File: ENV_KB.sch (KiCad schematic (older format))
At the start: 183 parts, among them J1 TYPE-C-31-M-12

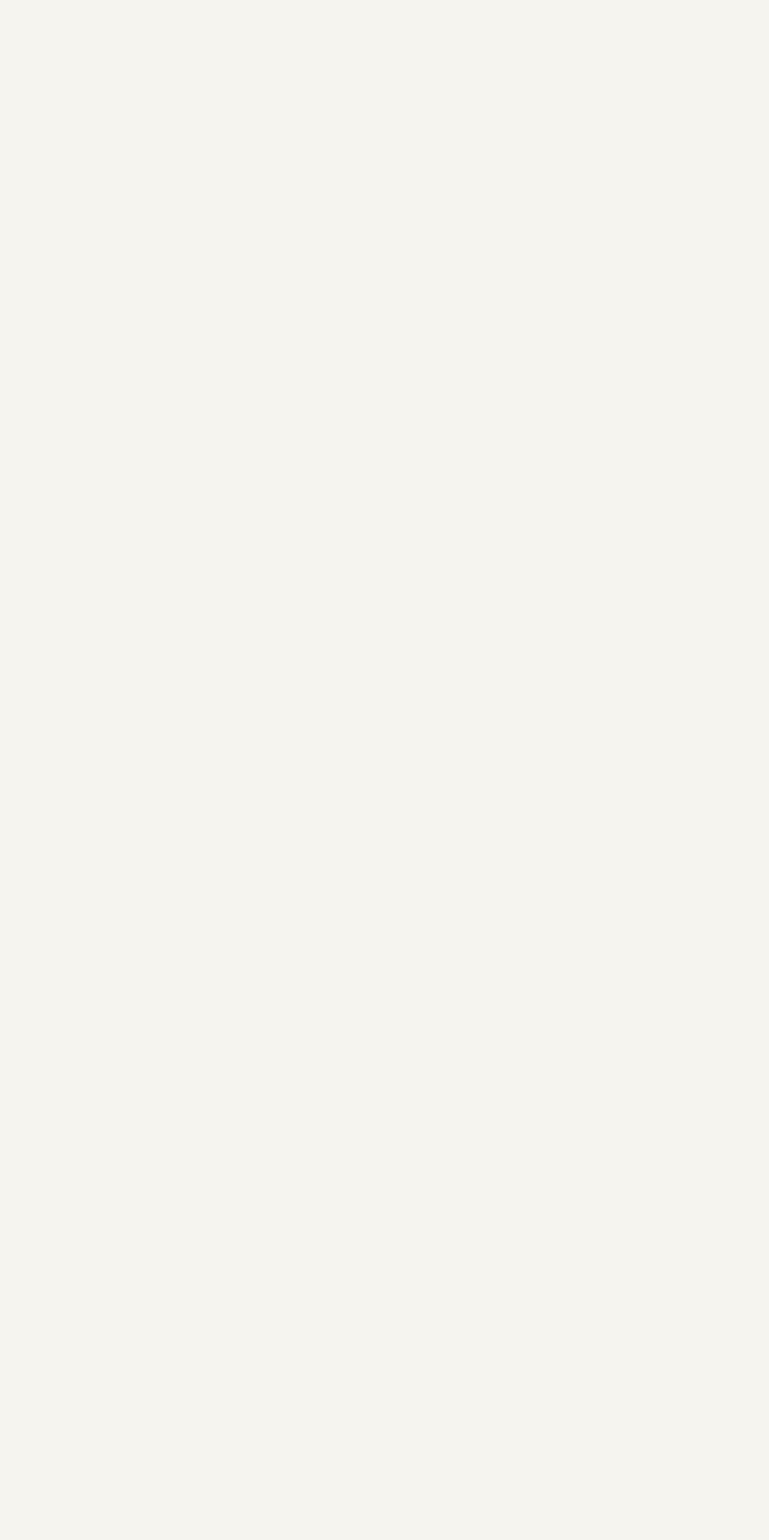
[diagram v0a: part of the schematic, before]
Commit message: Placing of the Keys and Track to the IO Expander Header for Spare Pin on IO Expander
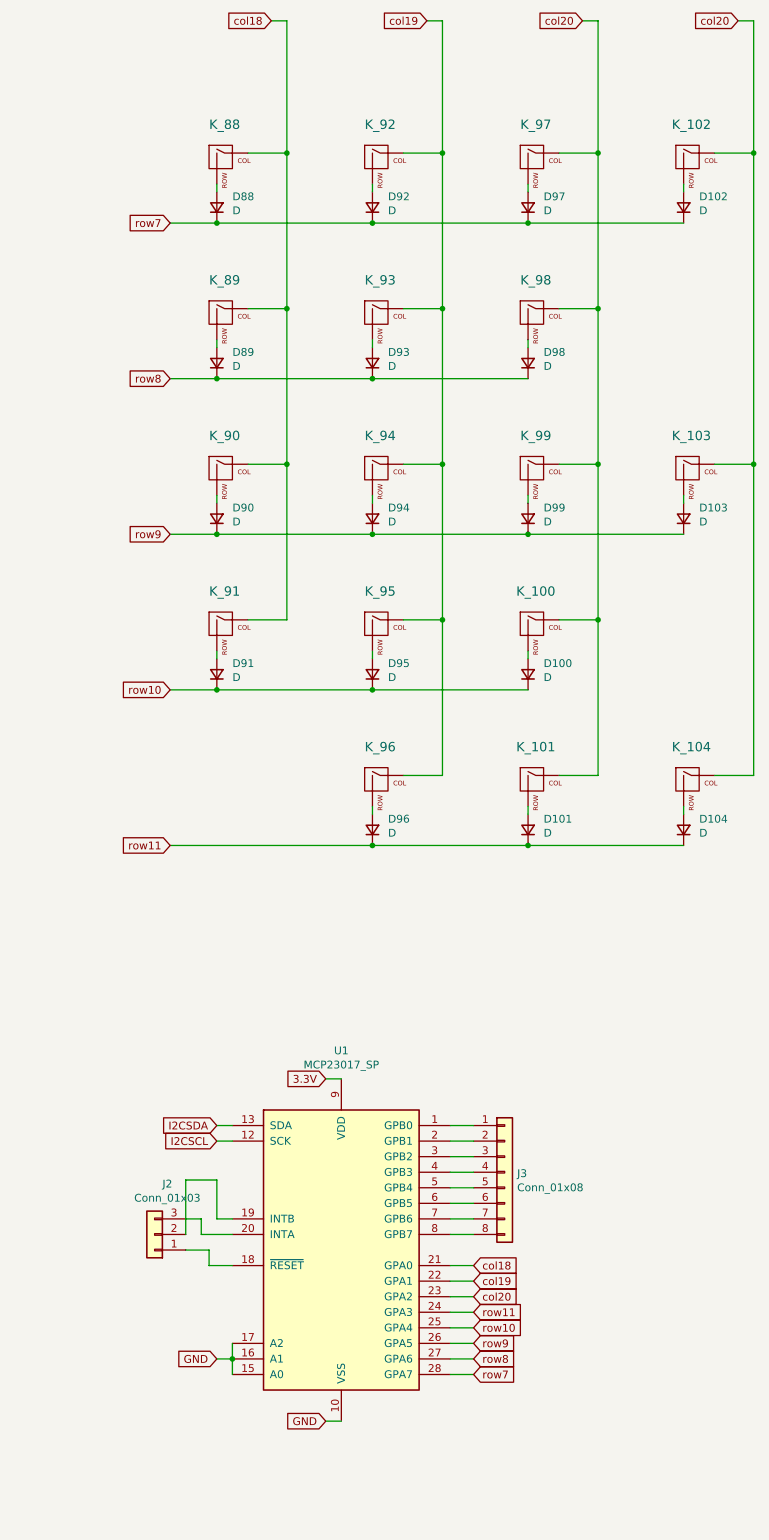
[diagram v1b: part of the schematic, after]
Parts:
- added D100, D101, D102, D103, D104, D88, D89, D90, D91, D92, D93, D94, D95, D96, D97, D98, D99: D, CFTKB Bits:D_DO-35_SOD27_P5.08mm_Horizontal, symbol Device:D_Small
- added J2: Conn_01x03, Connector_PinSocket_2.54mm:PinSocket_1x03_P2.54mm_Vertical, symbol Connector_Generic:Conn_01x03
- added J3: Conn_01x08, Connector_PinSocket_2.54mm:PinSocket_1x08_P2.54mm_Vertical, symbol Connector_Generic:Conn_01x08
- added K_100, K_101, K_102, K_89, K_90, K_91, K_92, K_93, K_94, K_95, K_97, K_98, K_99: KEYSW, MX_Only:MXOnly-1U-NoLED, symbol MX_Alps_Hybrid:MX-NoLED
- added K_103, K_104: KEYSW, MX_Only:MXOnly-2U-NoLED, symbol MX_Alps_Hybrid:MX-NoLED
- added K_88: Num Lock, MX_Only:MXOnly-1U-NoLED, symbol MX_Alps_Hybrid:MX-NoLED
- added K_96: KEYSW, MX_Only:MXOnly-2U-ReversedStabilizers-NoLED, symbol MX_Alps_Hybrid:MX-NoLED
- added U1: MCP23017_SP, Package_DIP:DIP-28_W7.62mm, symbol Interface_Expansion:MCP23017_SP
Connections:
- net 3.3V: now also U1.9 (VDD)
- net GND: now also U1.10 (VSS), U1.15 (A0), U1.16 (A1), U1.17 (A2)
- net I2CSCL: now also U1.12 (SCK)
- net I2CSDA: now also U1.13 (SDA)
- new net: D92.2 (A), K_92.2 (ROW)
- new net: D97.2 (A), K_97.2 (ROW)
- new net: D102.2 (A), K_102.2 (ROW)
- new net: D89.2 (A), K_89.2 (ROW)
- new net: D93.2 (A), K_93.2 (ROW)
- new net: D98.2 (A), K_98.2 (ROW)
- new net: D90.2 (A), K_90.2 (ROW)
- new net: D91.2 (A), K_91.2 (ROW)
- new net: D88.2 (A), K_88.2 (ROW)
- new net: D94.2 (A), K_94.2 (ROW)
- new net: D99.2 (A), K_99.2 (ROW)
- new net: D103.2 (A), K_103.2 (ROW)
- new net: D95.2 (A), K_95.2 (ROW)
- new net: D100.2 (A), K_100.2 (ROW)
- new net: D96.2 (A), K_96.2 (ROW)
- new net: D101.2 (A), K_101.2 (ROW)
- new net: D104.2 (A), K_104.2 (ROW)
- new net: J3.1 (Pin_1), U1.1 (GPB0)
- new net: J2.1 (Pin_1), U1.18 (~RESET~)
- new net: J2.2 (Pin_2), U1.19 (INTB)
- new net: J3.2 (Pin_2), U1.2 (GPB1)
- new net: J2.3 (Pin_3), U1.20 (INTA)
- new net: J3.3 (Pin_3), U1.3 (GPB2)
- new net: J3.4 (Pin_4), U1.4 (GPB3)
- new net: J3.5 (Pin_5), U1.5 (GPB4)
- new net: J3.6 (Pin_6), U1.6 (GPB5)
- new net: J3.7 (Pin_7), U1.7 (GPB6)
- new net: J3.8 (Pin_8), U1.8 (GPB7)
- new net col18: K_88.1 (COL), K_89.1 (COL), K_90.1 (COL), K_91.1 (COL), U1.21 (GPA0)
- new net col19: K_92.1 (COL), K_93.1 (COL), K_94.1 (COL), K_95.1 (COL), K_96.1 (COL), U1.22 (GPA1)
- new net col20: K_100.1 (COL), K_101.1 (COL), K_102.1 (COL), K_103.1 (COL), K_104.1 (COL), K_97.1 (COL), K_98.1 (COL), K_99.1 (COL), U1.23 (GPA2)
- new net row10: D100.1 (K), D91.1 (K), D95.1 (K), U1.25 (GPA4)
- new net row11: D101.1 (K), D104.1 (K), D96.1 (K), U1.24 (GPA3)
- new net row7: D102.1 (K), D88.1 (K), D92.1 (K), D97.1 (K), U1.28 (GPA7)
- new net row8: D89.1 (K), D93.1 (K), D98.1 (K), U1.27 (GPA6)
- new net row9: D103.1 (K), D90.1 (K), D94.1 (K), D99.1 (K), U1.26 (GPA5)

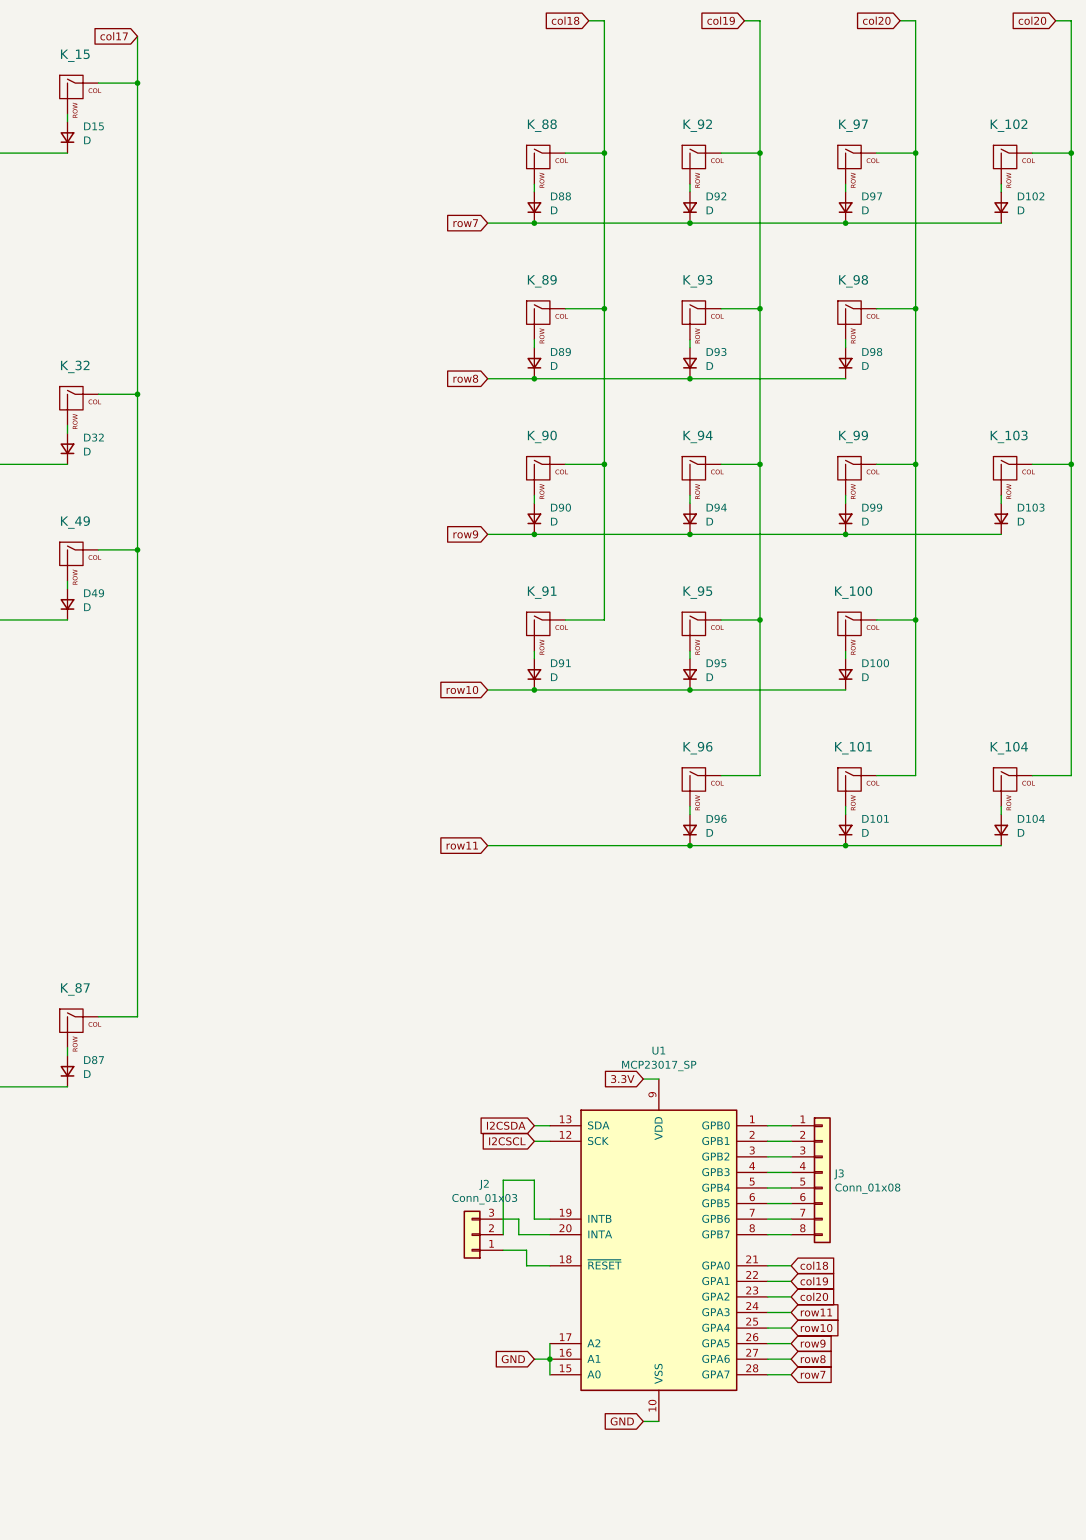
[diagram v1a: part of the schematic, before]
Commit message: Addtion of Solder Briges for Addresing of the Expander might re add an smaler one later Addtion of Pullups for I2C lines Removeal of Pinheader for IO Expander Fix Fuckup on Col 20 is used two times Fix some track tickness fails on col 21 Rerouting of some tracks
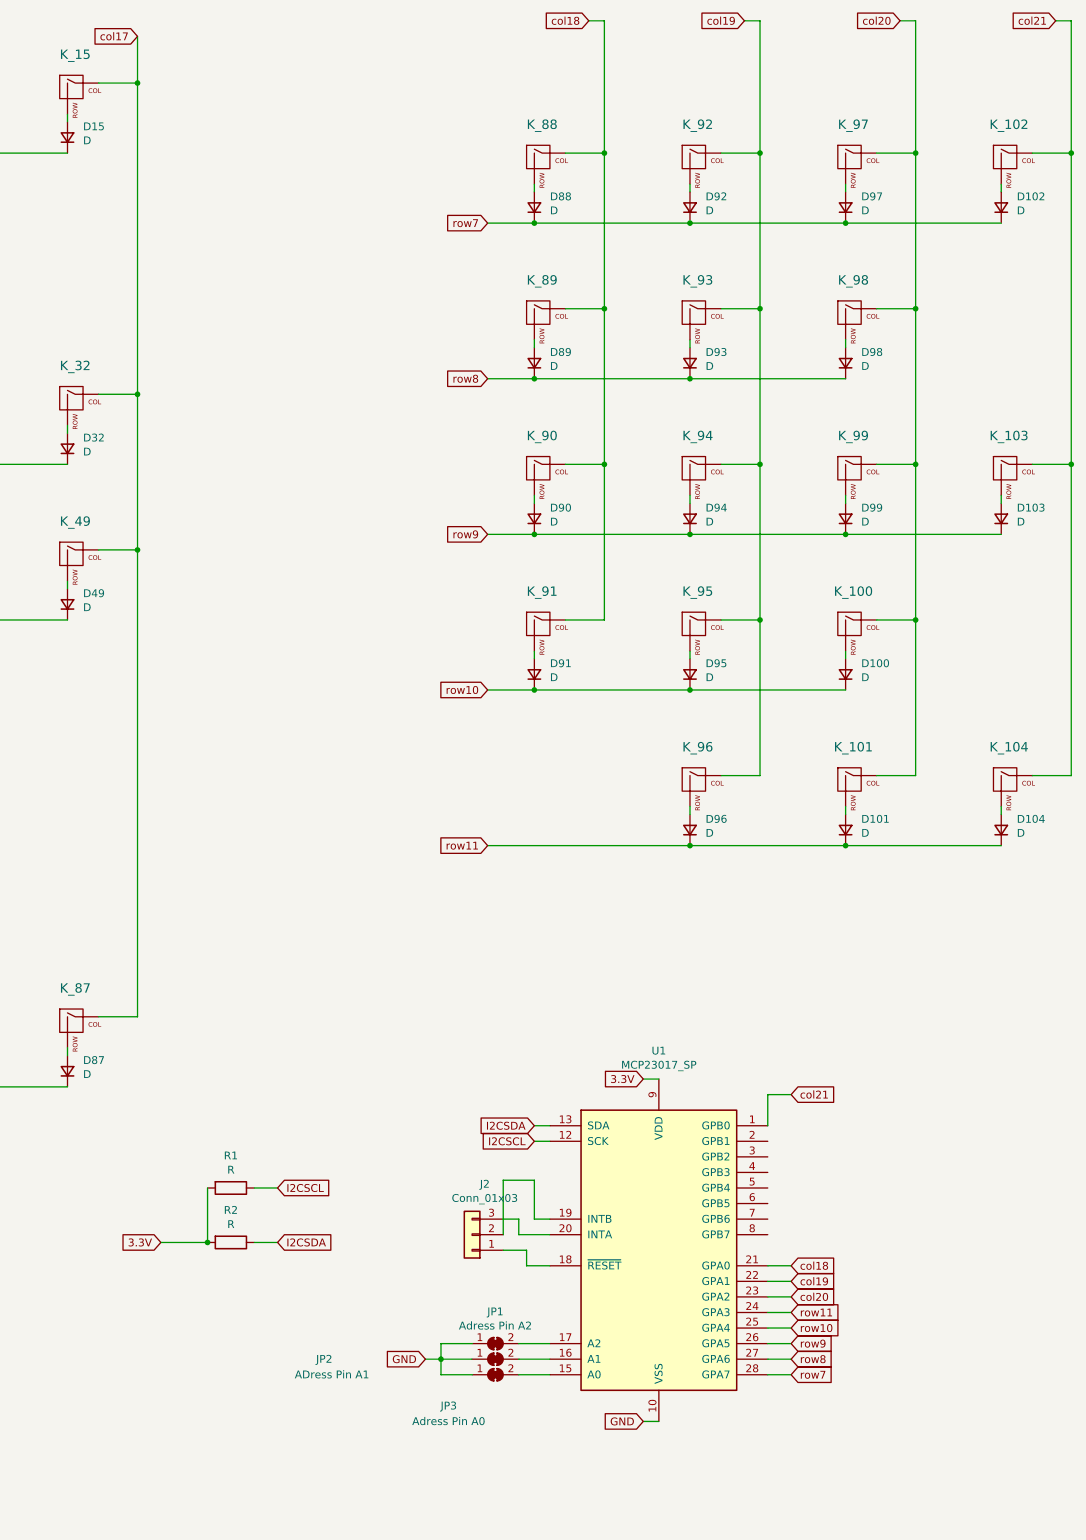
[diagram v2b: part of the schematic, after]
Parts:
- removed J3: Conn_01x08, Connector_PinSocket_2.54mm:PinSocket_1x08_P2.54mm_Vertical, symbol Connector_Generic:Conn_01x08
- added JP1: Adress Pin A2, Jumper:SolderJumper-2_P1.3mm_Bridged_RoundedPad1.0x1.5mm, symbol Jumper:SolderJumper_2_Bridged
- added JP2: ADress Pin A1, Jumper:SolderJumper-2_P1.3mm_Bridged_RoundedPad1.0x1.5mm, symbol Jumper:SolderJumper_2_Bridged
- added JP3: Adress Pin A0, Jumper:SolderJumper-2_P1.3mm_Bridged_RoundedPad1.0x1.5mm, symbol Jumper:SolderJumper_2_Bridged
- added R1, R2: R, CFTKB Bits:R_Axial_DIN0204_L3.6mm_D1.6mm_P7.62mm_Horizontal, symbol Device:R
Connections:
- net 3.3V: now also R1.2, R2.2
- net GND: now also JP1.1 (A), JP2.1 (A), JP3.1 (A); no longer U1.15 (A0), U1.16 (A1), U1.17 (A2)
- net I2CSCL: now also R1.1
- net I2CSDA: now also R2.1
- net col20: no longer K_102.1 (COL), K_103.1 (COL), K_104.1 (COL)
- net col21: now reaches U1.1 (GPB0)
- net col21: now also K_102.1 (COL), K_103.1 (COL), K_104.1 (COL)
- new net: JP1.2 (B), U1.17 (A2)
- new net: JP2.2 (B), U1.16 (A1)
- new net: JP3.2 (B), U1.15 (A0)
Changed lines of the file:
@@
 Wire Wire Line
 	22050 9550 22150 9550
-Wire Wire Line
-	21450 9050 21450 9150
-Connection ~ 21450 9150
-Wire Wire Line
-	21450 9150 21450 9250
-Wire Wire Line
-	21450 9150 21350 9150
-Text GLabel 21350 9150 0    50   Input ~ 0
+Text GLabel 20650 9150 0    50   Input ~ 0
 GND
 Text GLabel 23000 8550 2    50   Input ~ 0
@@
 col20
 Text GLabel 24700 550  0    50   Input ~ 0
-col20
+col21
 Wire Wire Line
 	24800 3400 24800 5400
@@
 Wire Wire Line
 	21300 8450 21150 8450
-$Comp
-L Connector_Generic:Conn_01x08 J3
-U 1 1 60DDE9A5
-P 23200 7950
-F 0 "J3" H 23280 7942 50  0000 L CNN
-F 1 "Conn_01x08" H 23280 7851 50  0000 L CNN
-F 2 "Connector_PinSocket_2.54mm:PinSocket_1x08_P2.54mm_Vertical" H 23200 7950 50  0001 C CNN
-F 3 "~" H 23200 7950 50  0001 C CNN
-	1    23200 7950
-	1    0    0    -1
-$EndComp
-Wire Wire Line
-	23000 7650 22850 7650
-Wire Wire Line
-	23000 7750 22850 7750
-Wire Wire Line
-	22850 7850 23000 7850
-Wire Wire Line
-	22850 7950 23000 7950
-Wire Wire Line
-	22850 8050 23000 8050
-Wire Wire Line
-	22850 8150 23000 8150
-Wire Wire Line
-	22850 8250 23000 8250
-Wire Wire Line
-	22850 8350 23000 8350
 Wire Wire Line
 	21250 8350 21250 8250
@@
 Wire Wire Line
 	21150 8000 21150 8350
+$Comp
+L Jumper:SolderJumper_2_Bridged JP1
+U 1 1 605A7E43
+P 21100 9050
+F 0 "JP1" H 21100 9255 50  0000 C CNN
+F 1 "Adress Pin A2" H 21100 9164 50  0000 C CNN
+F 2 "Jumper:SolderJumper-2_P1.3mm_Bridged_RoundedPad1.0x1.5mm" H 21100 9050 50  0001 C CNN
+F 3 "~" H 21100 9050 50  0001 C CNN
+	1    21100 9050
+	1    0    0    -1
+$EndComp
+$Comp
+L Jumper:SolderJumper_2_Bridged JP2
+U 1 1 605A8E6C
+P 21100 9150
+F 0 "JP2" H 20000 9150 50  0000 C CNN
+F 1 "ADress Pin A1" H 20050 9050 50  0000 C CNN
+F 2 "Jumper:SolderJumper-2_P1.3mm_Bridged_RoundedPad1.0x1.5mm" H 21100 9150 50  0001 C CNN
+F 3 "~" H 21100 9150 50  0001 C CNN
+	1    21100 9150
+	1    0    0    -1
+$EndComp
+$Comp
+L Jumper:SolderJumper_2_Bridged JP3
+U 1 1 605A94CB
+P 21100 9250
+F 0 "JP3" H 20800 9050 50  0000 C CNN
+F 1 "Adress Pin A0" H 20800 8950 50  0000 C CNN
+F 2 "Jumper:SolderJumper-2_P1.3mm_Bridged_RoundedPad1.0x1.5mm" H 21100 9250 50  0001 C CNN
+F 3 "~" H 21100 9250 50  0001 C CNN
+	1    21100 9250
+	1    0    0    -1
+$EndComp
+Wire Wire Line
+	20950 9050 20750 9050
+Wire Wire Line
+	20750 9050 20750 9150
+Wire Wire Line
+	20750 9150 20950 9150
+Wire Wire Line
+	20950 9250 20750 9250
+Wire Wire Line
+	20750 9250 20750 9150
+Connection ~ 20750 9150
+Wire Wire Line
+	21450 9250 21250 9250
+Wire Wire Line
+	21450 9150 21250 9150
+Wire Wire Line
+	21250 9050 21450 9050
+Wire Wire Line
+	20750 9150 20650 9150
+$Comp
+L Device:R R1
+U 1 1 607E1D31
+P 19400 8050
+F 0 "R1" V 19193 8050 50  0000 C CNN
+F 1 "R" V 19284 8050 50  0000 C CNN
+F 2 "CFTKB Bits:R_Axial_DIN0204_L3.6mm_D1.6mm_P7.62mm_Horizontal" V 19330 8050 50  0001 C CNN
+F 3 "~" H 19400 8050 50  0001 C CNN
+	1    19400 8050
+	0    1    1    0
+$EndComp
+$Comp
+L Device:R R2
+U 1 1 607E2C73
+P 19400 8400
+F 0 "R2" V 19193 8400 50  0000 C CNN
+F 1 "R" V 19284 8400 50  0000 C CNN
+F 2 "CFTKB Bits:R_Axial_DIN0204_L3.6mm_D1.6mm_P7.62mm_Horizontal" V 19330 8400 50  0001 C CNN
+F 3 "~" H 19400 8400 50  0001 C CNN
+	1    19400 8400
+	0    1    1    0
+$EndComp
+Text GLabel 19700 8050 2    50   Input ~ 0
+I2CSCL
+Text GLabel 19700 8400 2    50   Input ~ 0
+I2CSDA
+Wire Wire Line
+	19700 8050 19550 8050
+Wire Wire Line
+	19700 8400 19550 8400
+Wire Wire Line
+	19250 8050 19250 8400
+Wire Wire Line
+	18950 8400 19250 8400
+Connection ~ 19250 8400
+Text GLabel 18950 8400 0    50   Input ~ 0
+3.3V
+Text GLabel 23000 7450 2    50   Input ~ 0
+col21
+Wire Wire Line
+	23000 7450 22850 7450
+Wire Wire Line
+	22850 7450 22850 7650
 $EndSCHEMATC
